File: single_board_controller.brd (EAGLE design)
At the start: 160 x 100 mm, 82 parts, among them IC1 MCP3008, IC2 MCP3008, K1 AQ1AD2-3, K2 RELAY, P1 B9B-EH-A, Q1 NPN, Q2 NPN, Q3 NPN, Q4 NPN, Q5 NPN, Q6 NPN, Q7 TRANSISTIOR, Q8 TRANSISTIOR, T1 BTA41, U1 OPTOISOLATOR-2SOIC8, U2 OPTOISOLATOR-2SOIC8, U3 OPTOISOLATOR-2SOIC8, U4 OPTO-ISO

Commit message: placed the WOB header on brd, changed valve driver to two encoder headers, placed them on the brd
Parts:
- removed HL4, HL5: B2P-VH, con-jst-vh:B2P-VH
- removed Q5, Q6: NPN, SparkFun-DiscreteSemi:SOT23-3
- removed R13, R14, R15, R16: 10K, SparkFun-Resistors:0603-RES
- removed R17, R18: 220, SparkFun-Resistors:0603-RES
- removed STEPPER: (no value), SparkFun-Connectors:1X07
- removed U3: OPTOISOLATOR-2SOIC8, SparkFun-DiscreteSemi:SO08-2
- added ENC0, ENC1: (no value), SparkFun-Connectors:JST-3-PTH-VERT
- added P2: STEPPER, con-jst-eh:B6B-EH-A
- moved 12V_SUPPLY 73.2 mm to (50.2, 40.6)
- moved STEPPER_POWER 73.2 mm to (60.3, 40.6)
- moved 5V_SUPPLY 73.2 mm to (40.0, 40.6)
- moved WOB 19.1 mm to (125.1, 30.5)
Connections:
- removed net IN4: R17.1, RASPBERRRY_PI_3_B+.36
- removed net IN5: R18.1, RASPBERRRY_PI_3_B+.35
- removed net OUT1N2: Q6.1, R13.1, U3.8
- removed net OUT2N2: Q5.1, R14.1, U3.6
- removed net OUT4: HL4.2, Q6.3, R16.1
- removed net OUT5: HL5.2, Q5.3, R15.1
- net 12V: no longer R13.2, R14.2, R15.2, R16.2
- net 3.3V: now also ENC0.1, ENC1.1
- net DIR: now also P2.4, RASPBERRRY_PI_3_B+.35; no longer RASPBERRRY_PI_3_B+.40, STEPPER.5
- net GND: now also ENC0.2, ENC1.2, P2.1, P2.3, P2.5; no longer STEPPER.2, STEPPER.4, STEPPER.6, U3.2, U3.4
- net HV-GND: no longer HL4.1, HL5.1, Q5.2, Q6.2, U3.5, U3.7
- net N$5: now also ENC1.3, RASPBERRRY_PI_3_B+.37; no longer R17.2, U3.1
- net N$6: now also ENC0.3, RASPBERRRY_PI_3_B+.40; no longer R18.2, U3.3
- net STP: now also P2.6, RASPBERRRY_PI_3_B+.36; no longer RASPBERRRY_PI_3_B+.38, STEPPER.7
- net TIM: now also P2.2, RASPBERRRY_PI_3_B+.38; no longer RASPBERRRY_PI_3_B+.37, STEPPER.3
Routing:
- net DAT: track 0.00 -> 82.3 mm, vias 0 -> 1
- net N$6: track 0.00 -> 67.8 mm
- net N$5: track 0.00 -> 62.1 mm, vias 0 -> 1
- net 5V: track 0.00 -> 45.8 mm
- net CLK: track 0.00 -> 41.7 mm
- net CE0: track 97.8 -> 100.3 mm
- net CE1: track 62.2 -> 64.8 mm
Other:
- board size 160 x 100 mm -> 160 x 80.3 mm

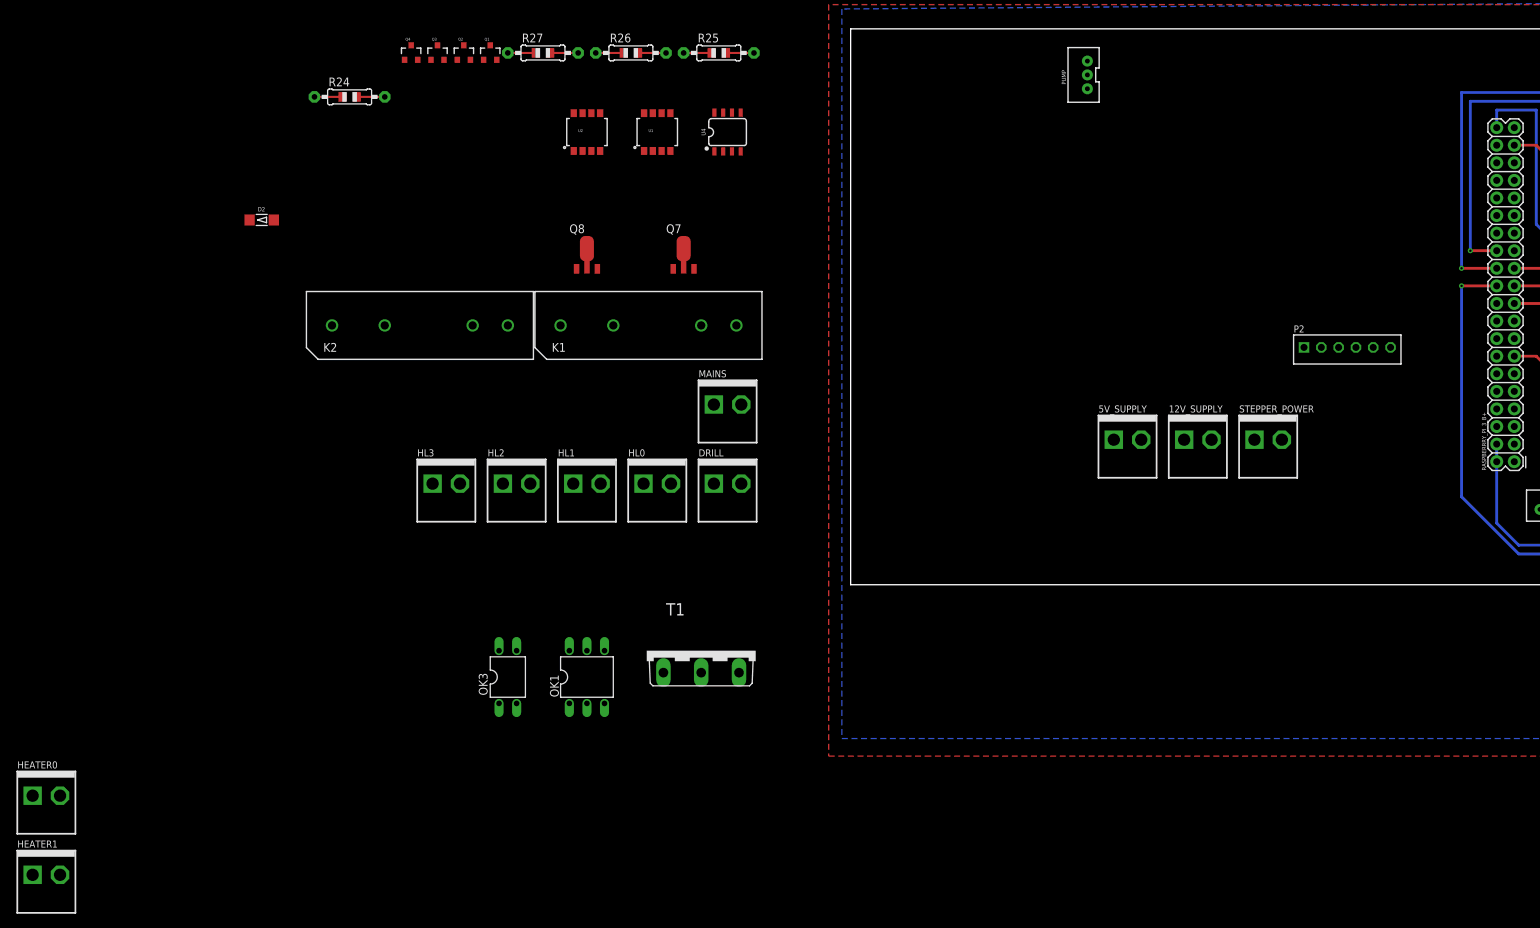
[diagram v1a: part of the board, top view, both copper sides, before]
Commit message: begun placing high power connectors
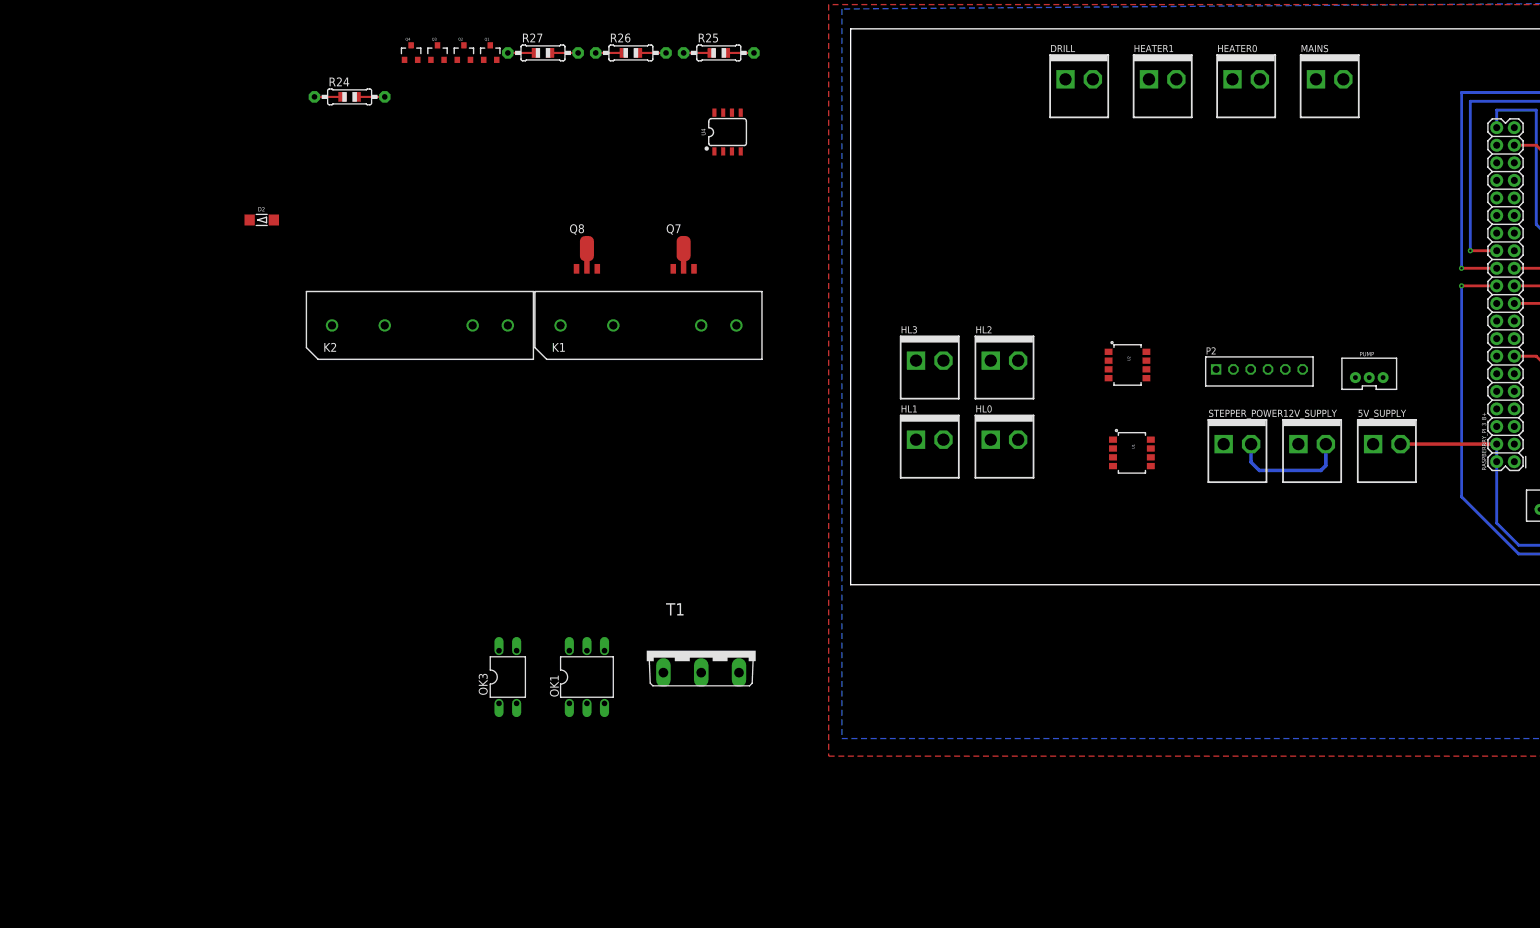
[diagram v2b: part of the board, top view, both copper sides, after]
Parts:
- moved HEATER0 201.9 mm to (57.1, 92.7)
- moved HEATER1 198.1 mm to (45.1, 92.7)
- moved MAINS 98.9 mm to (69.2, 92.7)
- moved U2 85.0 mm to (40.0, 51.4), turned to 270 degrees
- moved U1 82.8 mm to (40.6, 38.7), turned to 270 degrees
- moved DRILL 77.4 mm to (33.0, 92.7)
- moved HL2 72.7 mm to (22.2, 52.1)
- moved HL3 72.1 mm to (11.4, 52.1)
- moved PUMP 59.7 mm to (74.9, 50.2), turned to 0 degrees
- moved HL0 50.6 mm to (22.2, 40.6)
- moved HL1 49.9 mm to (11.4, 40.6)
- moved 5V_SUPPLY 37.5 mm to (77.5, 40.0)
- moved 12V_SUPPLY 16.5 mm to (66.7, 40.0)
- moved P2 13.1 mm to (59.1, 50.8)
- moved STEPPER_POWER 4.49 mm to (55.9, 40.0)
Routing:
- net 12V: track 0.00 -> 17.3 mm
- net 5V: track 45.8 -> 59.7 mm

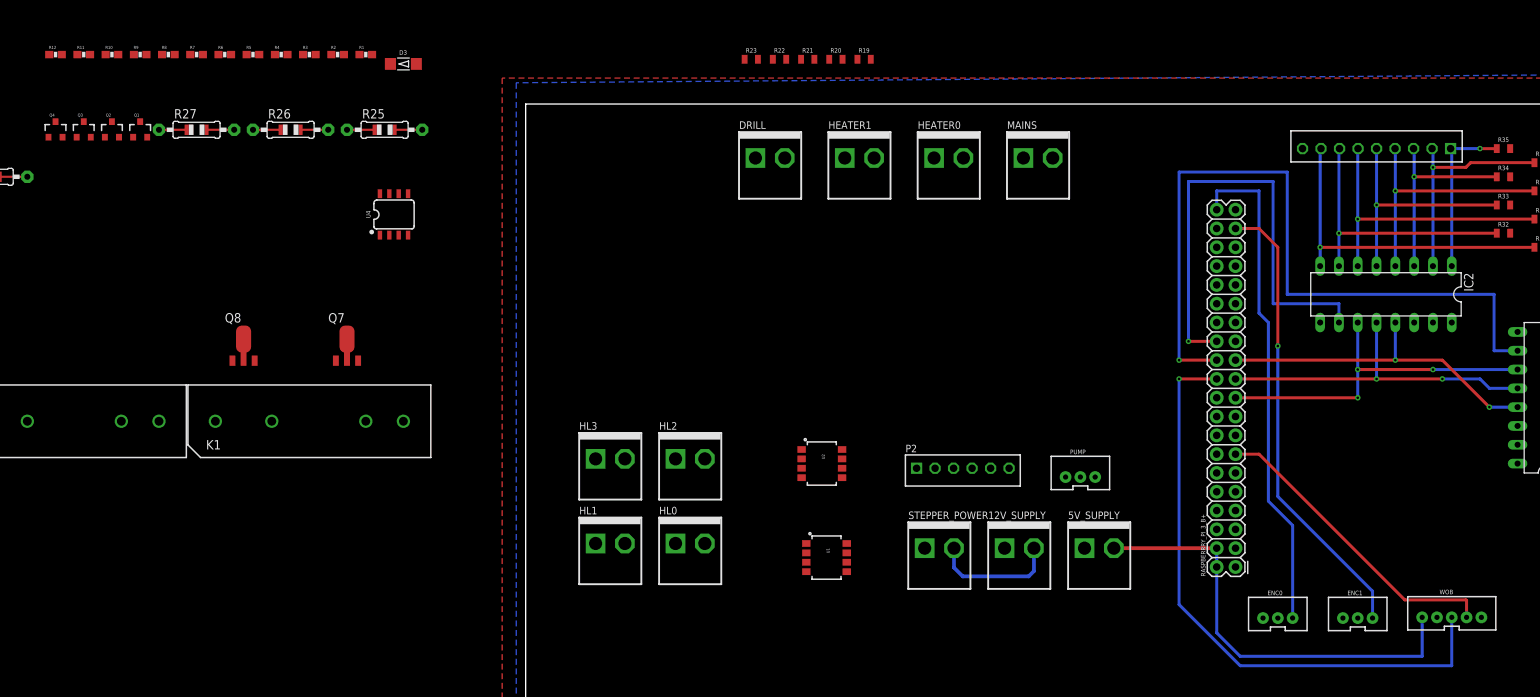
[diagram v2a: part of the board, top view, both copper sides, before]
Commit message: began adding 12V driver
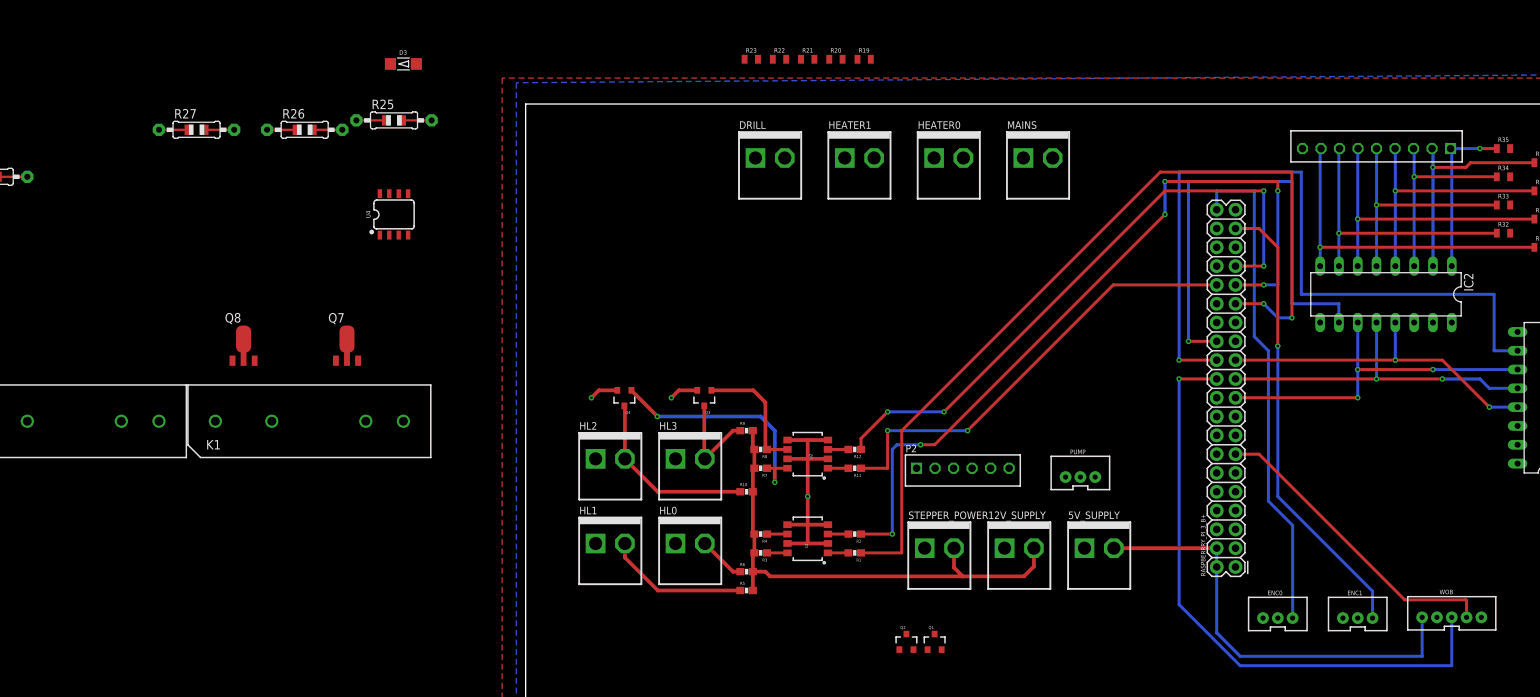
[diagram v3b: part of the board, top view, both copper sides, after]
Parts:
- moved Q1 127.7 mm to (55.2, 27.3)
- moved Q2 127.7 mm to (51.4, 27.3)
- moved R12 120.4 mm to (44.5, 53.3), turned to 180 degrees
- moved R11 118.2 mm to (44.5, 50.8), turned to 180 degrees
- moved R10 104.1 mm to (29.8, 47.6)
- moved R6 99.2 mm to (29.8, 36.8)
- moved R5 98.4 mm to (29.8, 34.3)
- moved R9 96.4 mm to (29.8, 55.9)
- moved R8 96.2 mm to (31.8, 53.3), turned to 180 degrees
- moved R2 95.3 mm to (44.5, 41.9), turned to 180 degrees
- moved R7 94.5 mm to (31.8, 50.8), turned to 180 degrees
- moved R1 94.3 mm to (44.5, 39.4), turned to 180 degrees
- moved R4 91.6 mm to (31.8, 41.9), turned to 180 degrees
- moved Q3 91.3 mm to (24.1, 60.3), turned to 180 degrees
- moved R3 90.8 mm to (31.8, 39.4), turned to 180 degrees
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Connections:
- removed net HV-GND: HL0.1, HL1.1, HL2.1, HL3.1, Q1.2, Q2.2, Q3.2, Q4.2, U1.5, U1.7, U2.5, U2.7
- net GND: now also HL0.1, HL1.1, HL2.1, HL3.1, Q1.2, Q2.2, Q3.2, Q4.2, U1.5, U1.7, U2.5, U2.7
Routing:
- net IN0: track 0.00 -> 117.3 mm, vias 0 -> 2
- net IN1: track 0.00 -> 105.0 mm, vias 0 -> 6
- net IN3: track 0.00 -> 83.7 mm, vias 0 -> 4
- net IN2: track 0.00 -> 61.5 mm, vias 0 -> 2
- net 12V: track 17.3 -> 68.2 mm
- net GND: track 0.00 -> 45.2 mm, vias 0 -> 3
- net OUT1N1: track 0.00 -> 33.3 mm, vias 0 -> 2
- net OUT2: track 0.00 -> 24.6 mm
- net OUT1: track 0.00 -> 19.3 mm
- net OUT2N1: track 0.00 -> 17.2 mm
- net OUT3: track 0.00 -> 13.6 mm
- net OUT0: track 0.00 -> 6.37 mm
- net OUT2N: track 0.00 -> 2.77 mm
- net OUT1N: track 0.00 -> 2.77 mm
- net N$4: track 0.00 -> 2.77 mm
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
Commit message: began cleaning up stencils
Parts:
- removed R24, R25, R26, R27: (no value), adafruit:0805-THM
- added B1: MB1S, rectifier:SOIC-4
- added R13, R14, R15, R16: 100, SparkFun-Resistors:0805
- moved D2 167.3 mm to (81.3, 55.2), flipped to the bottom, turned to 180 degrees
- moved OK3 143.7 mm to (69.8, 86.4), turned to 270 degrees
- moved OK1 138.6 mm to (69.8, 93.3), turned to 90 degrees
- moved D3 108.2 mm to (81.3, 59.1), flipped to the bottom, turned to 180 degrees
- moved T1 98.1 mm to (27.3, 95.2)
- moved Q8 97.8 mm to (59.7, 67.9), turned to 180 degrees
- moved K2 97.4 mm to (34.3, 69.8)
- moved U4 79.9 mm to (61.6, 75.6), turned to 90 degrees
- moved Q7 79.2 mm to (54.6, 75.6), turned to 180 degrees
- moved K1 68.2 mm to (34.3, 81.9)
- moved MAINS 59.7 mm to (9.53, 94.0)
- moved HEATER0 49.3 mm to (8.89, 82.5), turned to 90 degrees
- moved R22 47.0 mm to (78.7, 90.8)
- moved R21 44.6 mm to (78.7, 87.6)
- moved R23 42.8 mm to (65.4, 81.3), turned to 180 degrees
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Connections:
- removed net AC-H: MAINS.1, R19.2, R23.2, T1.A2
- removed net DIR: P2.4, PUMP.1, RASPBERRRY_PI_3_B+.15, RASPBERRRY_PI_3_B+.35
- new net N$24: B1.~2, MAINS.1, R23.2, T1.A2
- new net N$25: B1.~1, DRILL.1, MAINS.2
- new net N$26: B1.+, R19.2
- new net PDIR: PUMP.1, RASPBERRRY_PI_3_B+.15
- new net SDIR: P2.4, RASPBERRRY_PI_3_B+.35
- net AC-N: now also B1.-; no longer DRILL.1, MAINS.2
- net N$12: now also R13.2; no longer R24.2
- net N$13: now also R13.1; no longer R24.1
- net N$14: now also R14.2; no longer R26.2
- net N$15: now also R14.1; no longer R26.1
- net N$16: now also R15.1; no longer R25.1
- net N$17: now also R15.2; no longer R25.2
- net N$18: now also R16.1; no longer R27.1
- net N$19: now also R16.2; no longer R27.2
- net RELAY0: now also RASPBERRRY_PI_3_B+.16; no longer RASPBERRRY_PI_3_B+.18
- net RELAY1: now also RASPBERRRY_PI_3_B+.18; no longer RASPBERRRY_PI_3_B+.16
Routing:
- net INTERRUPT: track 0.00 -> 118.2 mm, vias 0 -> 6
- net CONTROL: track 0.00 -> 90.2 mm, vias 0 -> 5
- net SDIR: track 0.00 -> 86.7 mm, vias 0 -> 4
- net N$24: track 0.00 -> 75.2 mm
- net PDIR: track 0.00 -> 70.0 mm, vias 0 -> 2
- net GND: track 45.2 -> 110.7 mm, vias 3 -> 11
- net TIM: track 0.00 -> 51.5 mm
- net N$25: track 0.00 -> 48.2 mm
- net STP: track 0.00 -> 41.5 mm
- net OUT2N: track 2.77 -> 41.9 mm, vias 0 -> 2
- net N$10: track 0.00 -> 36.4 mm
- net N$11: track 0.00 -> 29.5 mm
- net N$13: track 0.00 -> 23.9 mm, vias 0 -> 1
- net N$15: track 0.00 -> 23.8 mm, vias 0 -> 1
- net HV0O: track 0.00 -> 23.4 mm
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
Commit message: added atiny85 drill driver, added mounting holes, isolated ground and 3.3V planes from AC, added I2C connector, still need to choose new mosfets, still need to verify AC circuitry, still need to pick appropriate resistors/capacitor/diodes
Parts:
- added C1: (no value), eagle-ltspice:C0805
- added I2C: (no value), SparkFun-Connectors:JST-4-PTH-VERT
- added R17, R18: 100, SparkFun-Resistors:0805
- added U$1: ATTINY85, attiny85:8P3
- moved R23 14.9 mm to (52.1, 87.9), turned to 90 degrees
- moved WOB 9.84 mm to (134.9, 30.5)
- moved DRILL 8.41 mm to (38.7, 93.0)
- moved R19 7.78 mm to (52.7, 95.6)
- moved R20 7.78 mm to (52.7, 92.4)
- moved B1 7.78 mm to (47.6, 92.4)
- moved OK1 7.33 mm to (62.5, 94.0)
- moved OK3 7.30 mm to (62.5, 86.4)
- moved R22 6.70 mm to (72.1, 91.4)
- moved R21 6.67 mm to (72.1, 87.6)
- moved T1 3.55 mm to (23.8, 95.9)
- moved D2 2.86 mm to (84.1, 55.2), flipped to the top, turned to 0 degrees
- moved D3 2.54 mm to (83.8, 59.1), flipped to the top, turned to 0 degrees
- renumbered STEPPER_POWER to STP_PWR
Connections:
- removed net INTERRUPT: OK3.4, R21.1, RASPBERRRY_PI_3_B+.7
- new net N$23: OK3.4, R21.1, U$1.7
- new net N$27: R22.2, U$1.5
- new net N$28: I2C.2, RASPBERRRY_PI_3_B+.5
- new net N$29: C1.1, R17.1, RASPBERRRY_PI_3_B+.7, U$1.3
- new net N$30: I2C.1, RASPBERRRY_PI_3_B+.3
- new net N$31: RASPBERRRY_PI_3_B+.10
- new net N$32: RASPBERRRY_PI_3_B+.8
- net 3.3V: now also I2C.4, U$1.8
- net CONTROL: now also R18.2, U$1.2; no longer R22.2
- net GND: now also C1.2, I2C.3, R17.2, R18.1, U$1.4
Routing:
- net INTERRUPT: track 118.2 -> 0.00 mm, vias 6 -> 0
- net N$29: track 0.00 -> 81.6 mm, vias 0 -> 3
- net N$28: track 0.00 -> 34.3 mm
- net N$30: track 0.00 -> 31.4 mm
- net GND: track 110.7 -> 141.7 mm, vias 11 -> 17
- net CLK: track 41.7 -> 58.4 mm
- net N$24: track 75.2 -> 58.6 mm
- net N$23: track 0.00 -> 15.4 mm
- net N$27: track 0.00 -> 14.8 mm
- net CONTROL: track 90.2 -> 104.1 mm, vias 5 -> 2
- net 5V: track 59.7 -> 69.5 mm
- net DAT: track 84.2 -> 93.1 mm
- net N$9: track 13.9 -> 22.1 mm
- net N$25: track 48.2 -> 41.3 mm
- net N$11: track 29.5 -> 24.0 mm
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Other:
- board size 160 x 80.3 mm -> 168.9 x 80.3 mm
